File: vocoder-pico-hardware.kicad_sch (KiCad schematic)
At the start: 54 parts, among them J1 Conn_02x05_Odd_Even, J2 AudioJack3_SwitchTR, J3 AudioJack3_SwitchTR, SW1 SW_Push, SW2 SW_Push, U1 TL072, U2 LM7805_TO220, U3 PCM5100A, U8 MCP6002-xMC

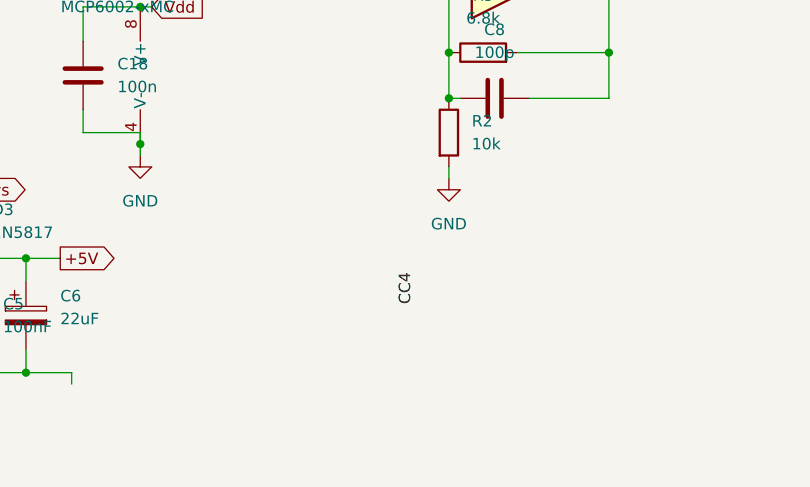
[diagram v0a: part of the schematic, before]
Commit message: finish footprints assignment
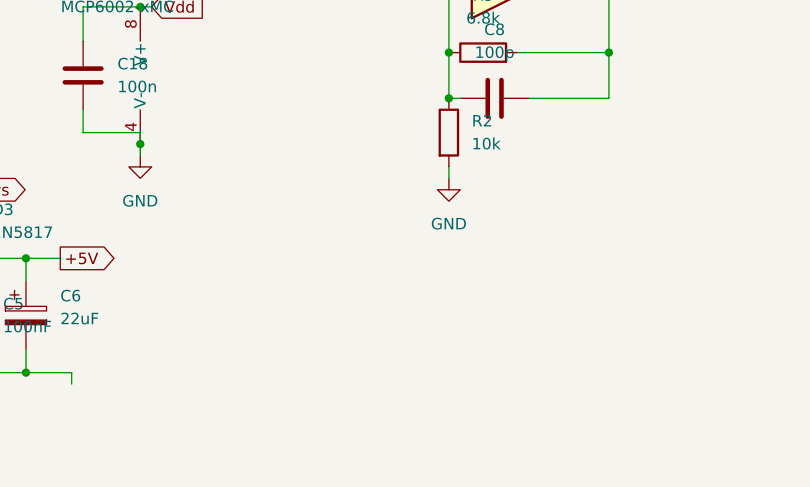
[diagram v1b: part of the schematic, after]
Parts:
- J1: footprint (none) -> Connector_IDC:IDC-Header_2x05_P2.54mm_Vertical
- J2, J3: footprint (none) -> Connector_Audio:Jack_3.5mm_QingPu_WQP-PJ398SM_Vertical_CircularHoles
- RV1, RV2: footprint (none) -> Potentiometer_THT:Potentiometer_Alpha_RD901F-40-00D_Single_Vertical
- U1: footprint (none) -> Package_DIP:DIP-8_W7.62mm_Socket
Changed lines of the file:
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@@
 		)
 	)
-	(label "CC4"
-		(at 185.42 177.8 90)
-		(effects
-			(font
-				(size 1.27 1.27)
-			)
-			(justify left bottom)
-		)
-	)
 	(global_label "GP8_SEG_G"
 		(shape output)
@@
 			)
 		)
-		(property "Footprint" ""
+		(property "Footprint" "Package_DIP:DIP-8_W7.62mm_Socket"
 			(at 77.47 180.34 0)
 			(effects
@@
 			)
 		)
-		(property "Footprint" ""
+		(property "Footprint" "Connector_Audio:Jack_3.5mm_QingPu_WQP-PJ398SM_Vertical_CircularHoles"
 			(at 27.94 140.97 0)
 			(effects
@@
 			)
 		)
-		(property "Footprint" ""
+		(property "Footprint" "Potentiometer_THT:Potentiometer_Alpha_RD901F-40-00D_Single_Vertical"
 			(at 180.34 71.12 0)
 			(effects
@@
 			)
 		)
-		(property "Footprint" ""
+		(property "Footprint" "Potentiometer_THT:Potentiometer_Alpha_RD901F-40-00D_Single_Vertical"
 			(at 158.75 72.39 0)
 			(effects
@@
 			)
 		)
-		(property "Footprint" ""
+		(property "Footprint" "Connector_IDC:IDC-Header_2x05_P2.54mm_Vertical"
 			(at 35.56 180.34 0)
 			(effects
@@
 			)
 		)
-		(property "Footprint" ""
+		(property "Footprint" "Package_DIP:DIP-8_W7.62mm_Socket"
 			(at 196.85 140.97 0)
 			(effects
@@
 			)
 		)
-		(property "Footprint" ""
+		(property "Footprint" "Connector_Audio:Jack_3.5mm_QingPu_WQP-PJ398SM_Vertical_CircularHoles"
 			(at 233.68 120.65 0)
 			(effects
@@
 			)
 		)
-		(property "Footprint" ""
+		(property "Footprint" "Package_DIP:DIP-8_W7.62mm_Socket"
 			(at 195.58 107.95 0)
 			(effects

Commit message: add footprints for capacitors
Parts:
- removed C8: 100p, symbol Device:C
- removed J2, J3: AudioJack3_SwitchTR, Connector_Audio:Jack_3.5mm_QingPu_WQP-PJ398SM_Vertical_CircularHoles, symbol Connector_Audio:AudioJack3_SwitchTR
- removed R2: 10k, Resistor_THT:R_Axial_DIN0207_L6.3mm_D2.5mm_P7.62mm_Horizontal, symbol Device:R
- removed R3: 6.8k, Resistor_THT:R_Axial_DIN0207_L6.3mm_D2.5mm_P7.62mm_Horizontal, symbol Device:R
- removed R6: 1k, Resistor_THT:R_Axial_DIN0207_L6.3mm_D2.5mm_P7.62mm_Horizontal, symbol Device:R
- removed unit 2 of U1
- added J2, J4: AudioJack2_SwitchT, symbol Connector_Audio:AudioJack2_SwitchT
- U8: value MCP6002-xMC -> MCP6002-xP; footprint Package_DFN_QFN:DFN-8-1EP_3x2mm_P0.5mm_EP1.75x1.45mm -> Package_DIP:DIP-8_W7.62mm_Socket
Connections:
- net GND: now also J2.S, J4.S
- net at C10.1: now also J4.T
- net at R5.2: now also J2.T
- no-connect marks 12 -> 10

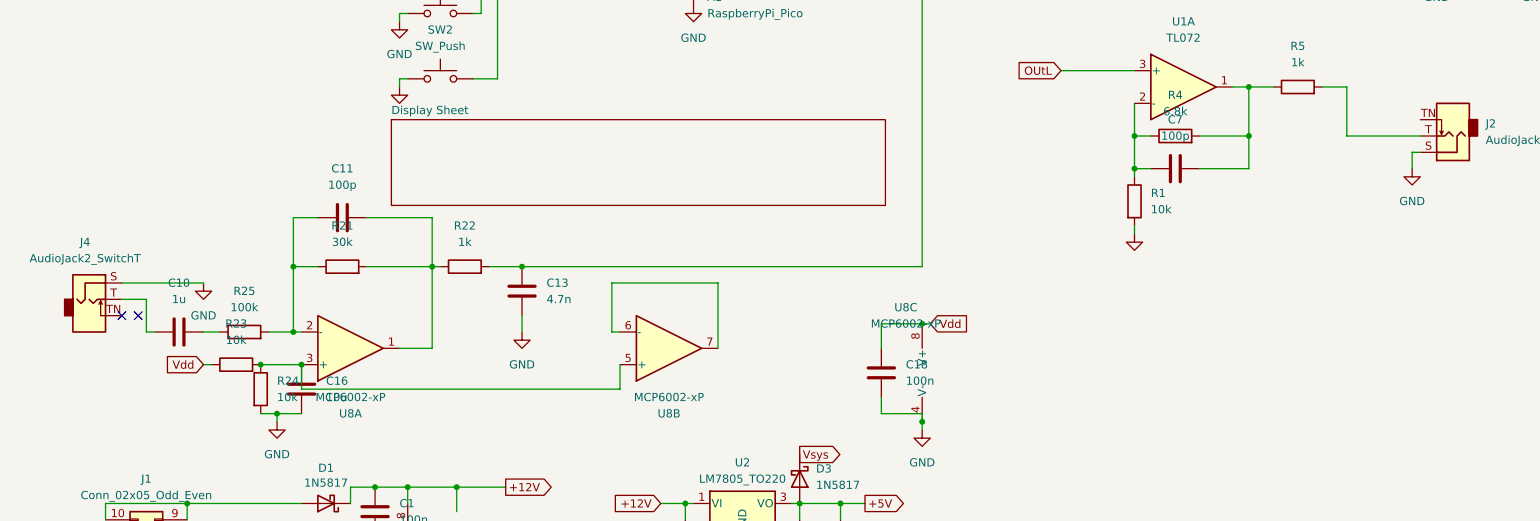
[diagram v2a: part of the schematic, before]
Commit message: more fixes for jacks and footprints
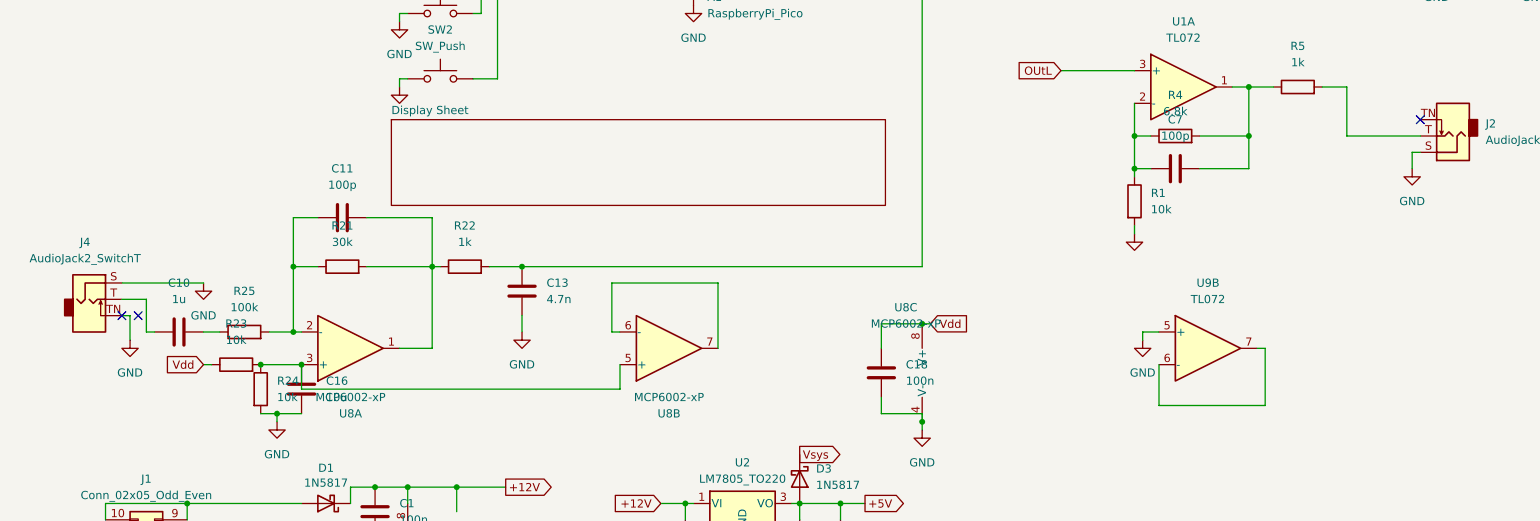
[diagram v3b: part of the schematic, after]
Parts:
- added U9: TL072, Package_DIP:DIP-8_W7.62mm_Socket, symbol Amplifier_Operational:TL072
- C1, C10, C11, C13, C14, C15, C16, C18, C19, C2, C20, C22, C23, C26, C28, C7: footprint (none) -> Capacitor_THT:C_Disc_D5.0mm_W2.5mm_P5.00mm
- J2, J4: footprint (none) -> Connector_Audio:Jack_3.5mm_QingPu_WQP-PJ398SM_Vertical_CircularHoles
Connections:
- net GND: now also J4.TN, U9.5 (+)
- new net: U9.6 (-), U9.7
- no-connect marks 10 -> 11

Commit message: final fixes
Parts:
- U8: value MCP6002-xP -> Amplifier_Operational:MCP6002-xP
- renumbered U9 to U1
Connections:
- no-connect marks 11 -> 9
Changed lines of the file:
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@@
 	)
 	(no_connect
-		(at 30.48 143.51)
-	)
-	(no_connect
 		(at 96.52 39.37)
 	)
 	(no_connect
-		(at 33.02 143.51)
-	)
-	(no_connect
 		(at 232.41 113.03)
 	)
@@
 	(wire
 		(pts
-			(xy 209.55 52.07) (xy 209.55 53.34)
+			(xy 30.48 143.51) (xy 31.75 143.51)
 		)
 		(stroke
@@
 	(wire
 		(pts
-			(xy 264.16 85.09) (xy 264.16 87.63)
+			(xy 209.55 52.07) (xy 209.55 53.34)
 		)
 		(stroke
@@
 	(wire
 		(pts
-			(xy 215.9 63.5) (xy 215.9 71.12)
+			(xy 264.16 85.09) (xy 264.16 87.63)
 		)
 		(stroke
@@
 	(wire
 		(pts
-			(xy 31.75 143.51) (xy 31.75 147.32)
+			(xy 215.9 63.5) (xy 215.9 71.12)
 		)
 		(stroke
@@
 	(wire
 		(pts
-			(xy 31.75 143.51) (xy 30.48 143.51)
-		)
-		(stroke
-			(width 0)
-			(type default)
-		)
-	)
-	(wire
-		(pts
 			(xy 247.65 63.5) (xy 250.19 63.5)
 		)
@@
 	(wire
 		(pts
+			(xy 31.75 143.51) (xy 31.75 147.32)
+		)
+		(stroke
+			(width 0)
+			(type default)
+		)
+	)
+	(wire
+		(pts
 			(xy 208.28 148.59) (xy 207.01 148.59)
 		)
@@
 			)
 		)
-		(property "Value" "MCP6002-xP"
+		(property "Value" "Amplifier_Operational:MCP6002-xP"
 			(at 66.04 156.21 0)
 			(effects
@@
 			)
 		)
-		(property "Value" "MCP6002-xP"
+		(property "Value" "Amplifier_Operational:MCP6002-xP"
 			(at 115.57 156.21 0)
 			(effects
@@
 		(dnp no)
 		(fields_autoplaced yes)
-		(property "Reference" "U9"
+		(property "Reference" "U1"
 			(at 199.39 138.43 0)
 			(effects
@@
 			(project "vocoder-pico-hardware"
 				(path "/68f2073a-7618-4fa5-a11d-b71bb4f75794"
-					(reference "U9")
+					(reference "U1")
 					(unit 2)
 				)
@@
 			)
 		)
-		(property "Value" "MCP6002-xP"
+		(property "Value" "Amplifier_Operational:MCP6002-xP"
 			(at 152.4 144.78 0)
 			(effects

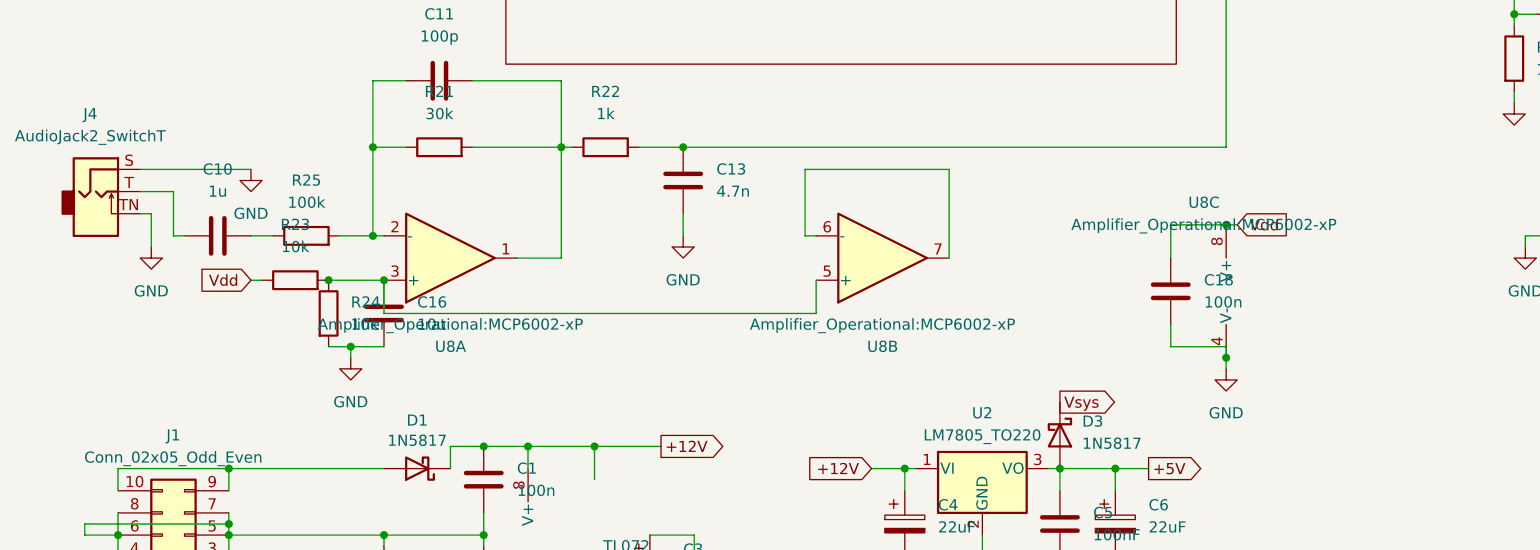
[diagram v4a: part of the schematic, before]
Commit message: fix wrong symbol
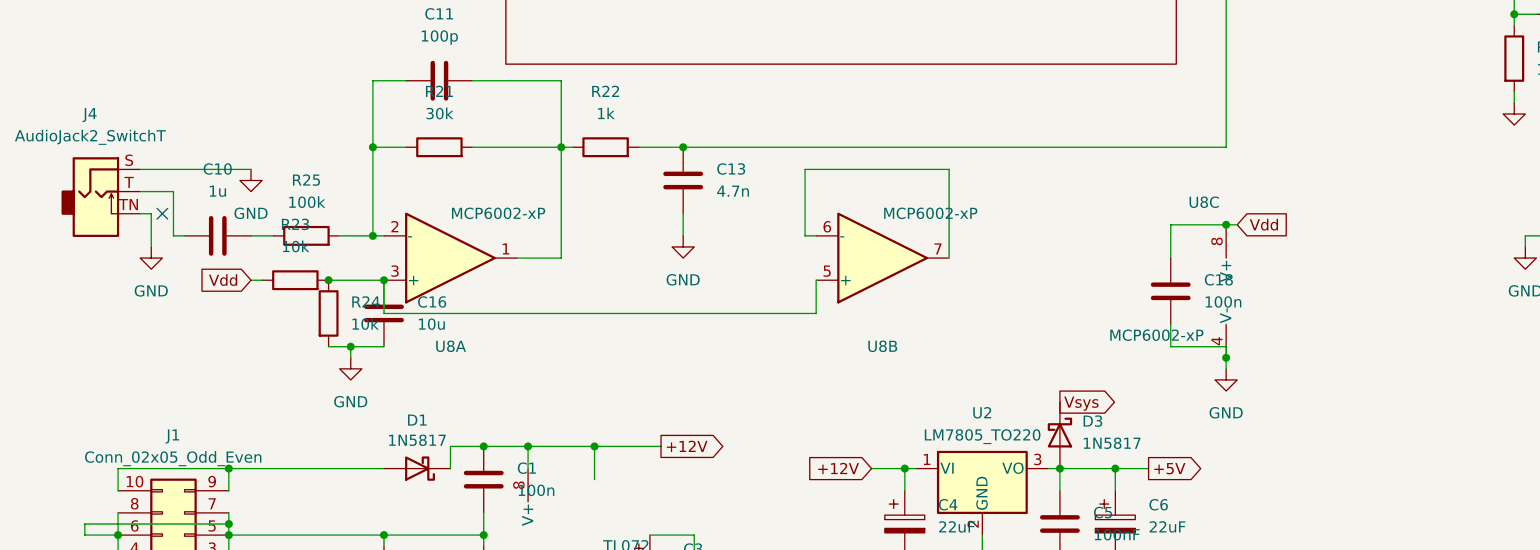
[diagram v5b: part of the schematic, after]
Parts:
- U8: value Amplifier_Operational:MCP6002-xP -> MCP6002-xP; symbol Amplifier_Operational:MCP6002-xMC -> Amplifier_Operational:MCP6002-xP
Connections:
- net GND: no longer U8.9 (V-)
- no-connect marks 9 -> 10
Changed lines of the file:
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@@
 	)
 	(no_connect
+		(at 33.02 143.51)
+	)
+	(no_connect
 		(at 232.41 113.03)
 	)
@@
 	(wire
 		(pts
-			(xy 30.48 143.51) (xy 31.75 143.51)
+			(xy 209.55 52.07) (xy 209.55 53.34)
 		)
 		(stroke
@@
 	(wire
 		(pts
-			(xy 209.55 52.07) (xy 209.55 53.34)
+			(xy 264.16 85.09) (xy 264.16 87.63)
 		)
 		(stroke
@@
 	(wire
 		(pts
-			(xy 264.16 85.09) (xy 264.16 87.63)
+			(xy 215.9 63.5) (xy 215.9 71.12)
 		)
 		(stroke
@@
 	(wire
 		(pts
-			(xy 215.9 63.5) (xy 215.9 71.12)
+			(xy 31.75 143.51) (xy 31.75 147.32)
 		)
 		(stroke
@@
 	(wire
 		(pts
+			(xy 30.48 143.51) (xy 31.75 143.51)
+		)
+		(stroke
+			(width 0)
+			(type default)
+		)
+	)
+	(wire
+		(pts
 			(xy 133.35 185.42) (xy 133.35 186.69)
 		)
@@
 	(wire
 		(pts
-			(xy 31.75 143.51) (xy 31.75 147.32)
-		)
-		(stroke
-			(width 0)
-			(type default)
-		)
-	)
-	(wire
-		(pts
 			(xy 208.28 148.59) (xy 207.01 148.59)
 		)
@@
 	)
 	(symbol
-		(lib_id "Amplifier_Operational:MCP6002-xMC")
+		(lib_id "Amplifier_Operational:MCP6002-xP")
 		(at 66.04 148.59 0)
 		(mirror x)
@@
 			)
 		)
-		(property "Value" "Amplifier_Operational:MCP6002-xP"
-			(at 66.04 156.21 0)
+		(property "Value" "MCP6002-xP"
+			(at 66.04 143.51 0)
 			(effects
 				(font
 					(size 1.27 1.27)
 				)
+				(justify left)
 			)
 		)
@@
 			)
 		)
-		(property "Description" "1MHz, Low-Power Op Amp, DFN-8"
+		(property "Description" "1MHz, Low-Power Op Amp, DIP-8"
 			(at 66.04 148.59 0)
 			(effects
@@
 			)
 		)
-		(pin "9"
-		)
 		(pin "7"
 		)
@@
 	)
 	(symbol
-		(lib_id "Amplifier_Operational:MCP6002-xMC")
+		(lib_id "Amplifier_Operational:MCP6002-xP")
 		(at 115.57 148.59 0)
 		(mirror x)
@@
 			)
 		)
-		(property "Value" "Amplifier_Operational:MCP6002-xP"
-			(at 115.57 156.21 0)
+		(property "Value" "MCP6002-xP"
+			(at 115.57 143.51 0)
 			(effects
 				(font
 					(size 1.27 1.27)
 				)
+				(justify left)
 			)
 		)
@@
 			)
 		)
-		(property "Description" "1MHz, Low-Power Op Amp, DFN-8"
+		(property "Description" "1MHz, Low-Power Op Amp, DIP-8"
 			(at 115.57 148.59 0)
 			(effects
@@
 			)
 		)
-		(pin "9"
-		)
 		(pin "7"
 		)
@@
 	)
 	(symbol
-		(lib_id "Amplifier_Operational:MCP6002-xMC")
+		(lib_id "Amplifier_Operational:MCP6002-xP")
 		(at 152.4 152.4 0)
 		(mirror y)
@@
 			)
 		)
-		(property "Value" "Amplifier_Operational:MCP6002-xP"
-			(at 152.4 144.78 0)
+		(property "Value" "MCP6002-xP"
+			(at 152.4 157.48 0)
 			(effects
 				(font
 					(size 1.27 1.27)
 				)
+				(justify left)
 			)
 		)
@@
 			)
 		)
-		(property "Description" "1MHz, Low-Power Op Amp, DFN-8"
+		(property "Description" "1MHz, Low-Power Op Amp, DIP-8"
 			(at 152.4 152.4 0)
 			(effects
@@
 			)
 		)
-		(pin "9"
-		)
 		(pin "7"

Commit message: adding edge.cuts and placing components
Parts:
- renumbered J4 to J2, J2 to J3
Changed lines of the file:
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@@
 		(dnp no)
 		(fields_autoplaced yes)
-		(property "Reference" "J4"
+		(property "Reference" "J2"
 			(at 24.765 132.08 0)
 			(effects
@@
 			(project "vocoder-pico-hardware"
 				(path "/68f2073a-7618-4fa5-a11d-b71bb4f75794"
-					(reference "J4")
+					(reference "J2")
 					(unit 1)
 				)
@@
 		(dnp no)
 		(fields_autoplaced yes)
-		(property "Reference" "J2"
+		(property "Reference" "J3"
 			(at 242.57 113.6649 0)
 			(effects
@@
 			(project ""
 				(path "/68f2073a-7618-4fa5-a11d-b71bb4f75794"
-					(reference "J2")
-					(unit 1)
-				)
+					(reference "J3")
+					(unit 1)
+				)

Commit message: replace certain resistor with 0805
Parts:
- R1, R21, R22, R23, R24, R25, R4, R7, R8: footprint Resistor_THT:R_Axial_DIN0207_L6.3mm_D2.5mm_P7.62mm_Horizontal -> Resistor_SMD:R_0805_2012Metric
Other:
- moved on the sheet: C7, R1
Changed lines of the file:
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@@
 	)
 	(junction
-		(at 187.96 120.65)
+		(at 91.44 189.23)
 		(diameter 0)
 		(color 0 0 0 0)
 	)
 	(junction
-		(at 91.44 189.23)
+		(at 187.96 125.73)
 		(diameter 0)
 		(color 0 0 0 0)
@@
 	(wire
 		(pts
-			(xy 198.12 120.65) (xy 205.74 120.65)
+			(xy 198.12 125.73) (xy 205.74 125.73)
 		)
 		(stroke
@@
 	(wire
 		(pts
+			(xy 205.74 115.57) (xy 205.74 125.73)
+		)
+		(stroke
+			(width 0)
+			(type default)
+		)
+	)
+	(wire
+		(pts
 			(xy 34.29 140.97) (xy 34.29 146.05)
 		)
@@
 	(wire
 		(pts
-			(xy 187.96 115.57) (xy 187.96 120.65)
+			(xy 187.96 115.57) (xy 187.96 125.73)
 		)
 		(stroke
@@
 	(wire
 		(pts
-			(xy 187.96 130.81) (xy 187.96 129.54)
+			(xy 187.96 135.89) (xy 187.96 134.62)
 		)
 		(stroke
@@
 	(wire
 		(pts
-			(xy 205.74 115.57) (xy 205.74 120.65)
-		)
-		(stroke
-			(width 0)
-			(type default)
-		)
-	)
-	(wire
-		(pts
 			(xy 40.64 175.26) (xy 40.64 172.72)
 		)
@@
 	(wire
 		(pts
-			(xy 187.96 120.65) (xy 187.96 121.92)
+			(xy 187.96 125.73) (xy 187.96 127)
 		)
 		(stroke
@@
 	(wire
 		(pts
-			(xy 187.96 120.65) (xy 190.5 120.65)
+			(xy 187.96 125.73) (xy 190.5 125.73)
 		)
 		(stroke
@@
 			)
 		)
-		(property "Footprint" "Resistor_THT:R_Axial_DIN0207_L6.3mm_D2.5mm_P7.62mm_Horizontal"
+		(property "Footprint" "Resistor_SMD:R_0805_2012Metric"
 			(at 83.82 137.668 90)
 			(effects
@@
 	(symbol
 		(lib_id "Device:C")
-		(at 194.31 120.65 90)
+		(at 194.31 125.73 90)
 		(unit 1)
 		(exclude_from_sim no)
@@
 		(fields_autoplaced yes)
 		(property "Reference" "C7"
-			(at 194.31 113.03 90)
+			(at 194.31 118.11 90)
 			(effects
 				(font
@@
 		)
 		(property "Value" "100p"
-			(at 194.31 115.57 90)
+			(at 194.31 120.65 90)
 			(effects
 				(font
@@
 		)
 		(property "Footprint" "Capacitor_THT:C_Disc_D5.0mm_W2.5mm_P5.00mm"
-			(at 198.12 119.6848 0)
+			(at 198.12 124.7648 0)
 			(effects
 				(font
@@
 		)
 		(property "Datasheet" "~"
-			(at 194.31 120.65 0)
+			(at 194.31 125.73 0)
 			(effects
 				(font
@@
 		)
 		(property "Description" "Unpolarized capacitor"
-			(at 194.31 120.65 0)
+			(at 194.31 125.73 0)
 			(effects
 				(font
@@
 			)
 		)
-		(property "Footprint" "Resistor_THT:R_Axial_DIN0207_L6.3mm_D2.5mm_P7.62mm_Horizontal"
+		(property "Footprint" "Resistor_SMD:R_0805_2012Metric"
 			(at 50.292 154.94 90)
 			(effects
@@
 			)
 		)
-		(property "Footprint" "Resistor_THT:R_Axial_DIN0207_L6.3mm_D2.5mm_P7.62mm_Horizontal"
+		(property "Footprint" "Resistor_SMD:R_0805_2012Metric"
 			(at 194.31 117.348 90)
 			(effects
@@
 			)
 		)
-		(property "Footprint" "Resistor_THT:R_Axial_DIN0207_L6.3mm_D2.5mm_P7.62mm_Horizontal"
+		(property "Footprint" "Resistor_SMD:R_0805_2012Metric"
 			(at 48.26 152.908 90)
 			(effects
@@
 	(symbol
 		(lib_id "Device:R")
-		(at 187.96 125.73 0)
+		(at 187.96 130.81 0)
 		(unit 1)
 		(exclude_from_sim no)
@@
 		(fields_autoplaced yes)
 		(property "Reference" "R1"
-			(at 190.5 124.4599 0)
+			(at 190.5 129.5399 0)
 			(effects
 				(font
@@
 		)
 		(property "Value" "10k"
-			(at 190.5 126.9999 0)
+			(at 190.5 132.0799 0)
 			(effects
 				(font
@@
 			)
 		)
-		(property "Footprint" "Resistor_THT:R_Axial_DIN0207_L6.3mm_D2.5mm_P7.62mm_Horizontal"
-			(at 186.182 125.73 90)
+		(property "Footprint" "Resistor_SMD:R_0805_2012Metric"
+			(at 186.182 130.81 90)
 			(effects
 				(font
@@
 		)
 		(property "Datasheet" "~"
-			(at 187.96 125.73 0)
+			(at 187.96 130.81 0)
 			(effects
 				(font
@@
 		)
 		(property "Description" "Resistor"
-			(at 187.96 125.73 0)
+			(at 187.96 130.81 0)
 			(effects
 				(font
@@
 			)
 		)
-		(property "Footprint" "Resistor_THT:R_Axial_DIN0207_L6.3mm_D2.5mm_P7.62mm_Horizontal"
+		(property "Footprint" "Resistor_SMD:R_0805_2012Metric"
 			(at 64.77 137.668 90)
 			(effects
@@
 			)
 		)
-		(property "Footprint" "Resistor_THT:R_Axial_DIN0207_L6.3mm_D2.5mm_P7.62mm_Horizontal"
+		(property "Footprint" "Resistor_SMD:R_0805_2012Metric"
 			(at 49.53 147.828 90)
 			(effects
@@
 			)
 		)
-		(property "Footprint" "Resistor_THT:R_Axial_DIN0207_L6.3mm_D2.5mm_P7.62mm_Horizontal"
+		(property "Footprint" "Resistor_SMD:R_0805_2012Metric"
 			(at 254 57.658 90)
 			(effects
@@
 	(symbol
 		(lib_id "power:GND")
-		(at 187.96 130.81 0)
+		(at 187.96 135.89 0)
 		(unit 1)
 		(exclude_from_sim no)
@@
 		(fields_autoplaced yes)
 		(property "Reference" "#PWR08"
-			(at 187.96 137.16 0)
+			(at 187.96 142.24 0)
 			(effects
 				(font
@@
 		)
 		(property "Value" "GND"
-			(at 187.96 135.89 0)
+			(at 187.96 140.97 0)
 			(effects
 				(font
@@
 		)
 		(property "Footprint" ""
-			(at 187.96 130.81 0)
+			(at 187.96 135.89 0)
 			(effects
 				(font
@@
 		)
 		(property "Datasheet" ""
-			(at 187.96 130.81 0)
+			(at 187.96 135.89 0)
 			(effects
 				(font
@@
 		)
 		(property "Description" "Power symbol creates a global label with name \"GND\" , ground"
-			(at 187.96 130.81 0)
+			(at 187.96 135.89 0)
 			(effects
 				(font
@@
 			)
 		)
-		(property "Footprint" "Resistor_THT:R_Axial_DIN0207_L6.3mm_D2.5mm_P7.62mm_Horizontal"
+		(property "Footprint" "Resistor_SMD:R_0805_2012Metric"
 			(at 254 60.198 90)
 			(effects
